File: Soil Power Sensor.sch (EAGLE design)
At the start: 95 parts, among them J1 12401832E402A, U10 TPS7A20330PDBVR, U11 TPS60403DBVR, U12 REF1933AIDDCR, U13 TLV1117LV33DCYR, U14 FSA2466UMX, U2 FT234XD-R, U3 MAX9944ATA+T, U4 ESP32-C3-MINI-1-N4, U5 LTC6362CDDPBF, U6 LTC6362CDDPBF, U7 INA296A5, U8 MAX11201AEUB+, U9 MAX11201AEUB+, X1 SMA-142-0701-801/806

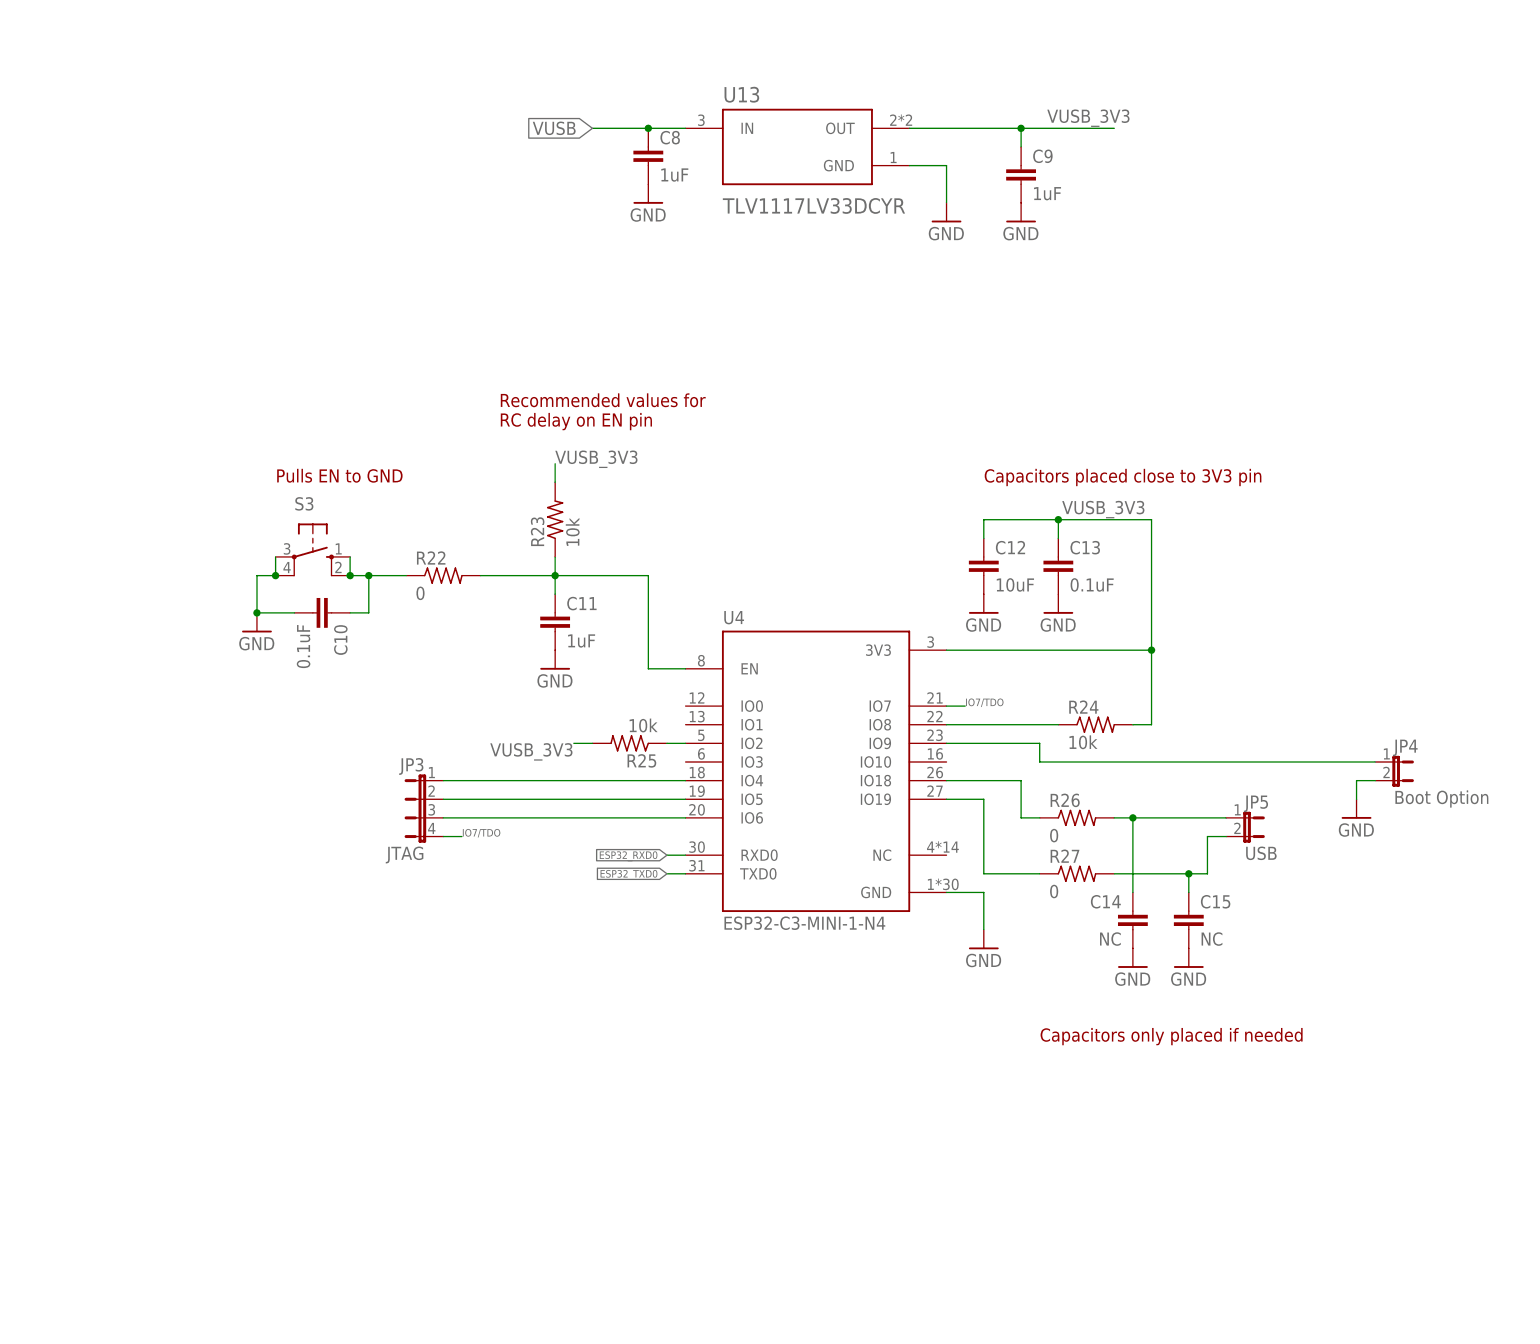
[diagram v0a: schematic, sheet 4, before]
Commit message: Updated JTAG connector for ESP32
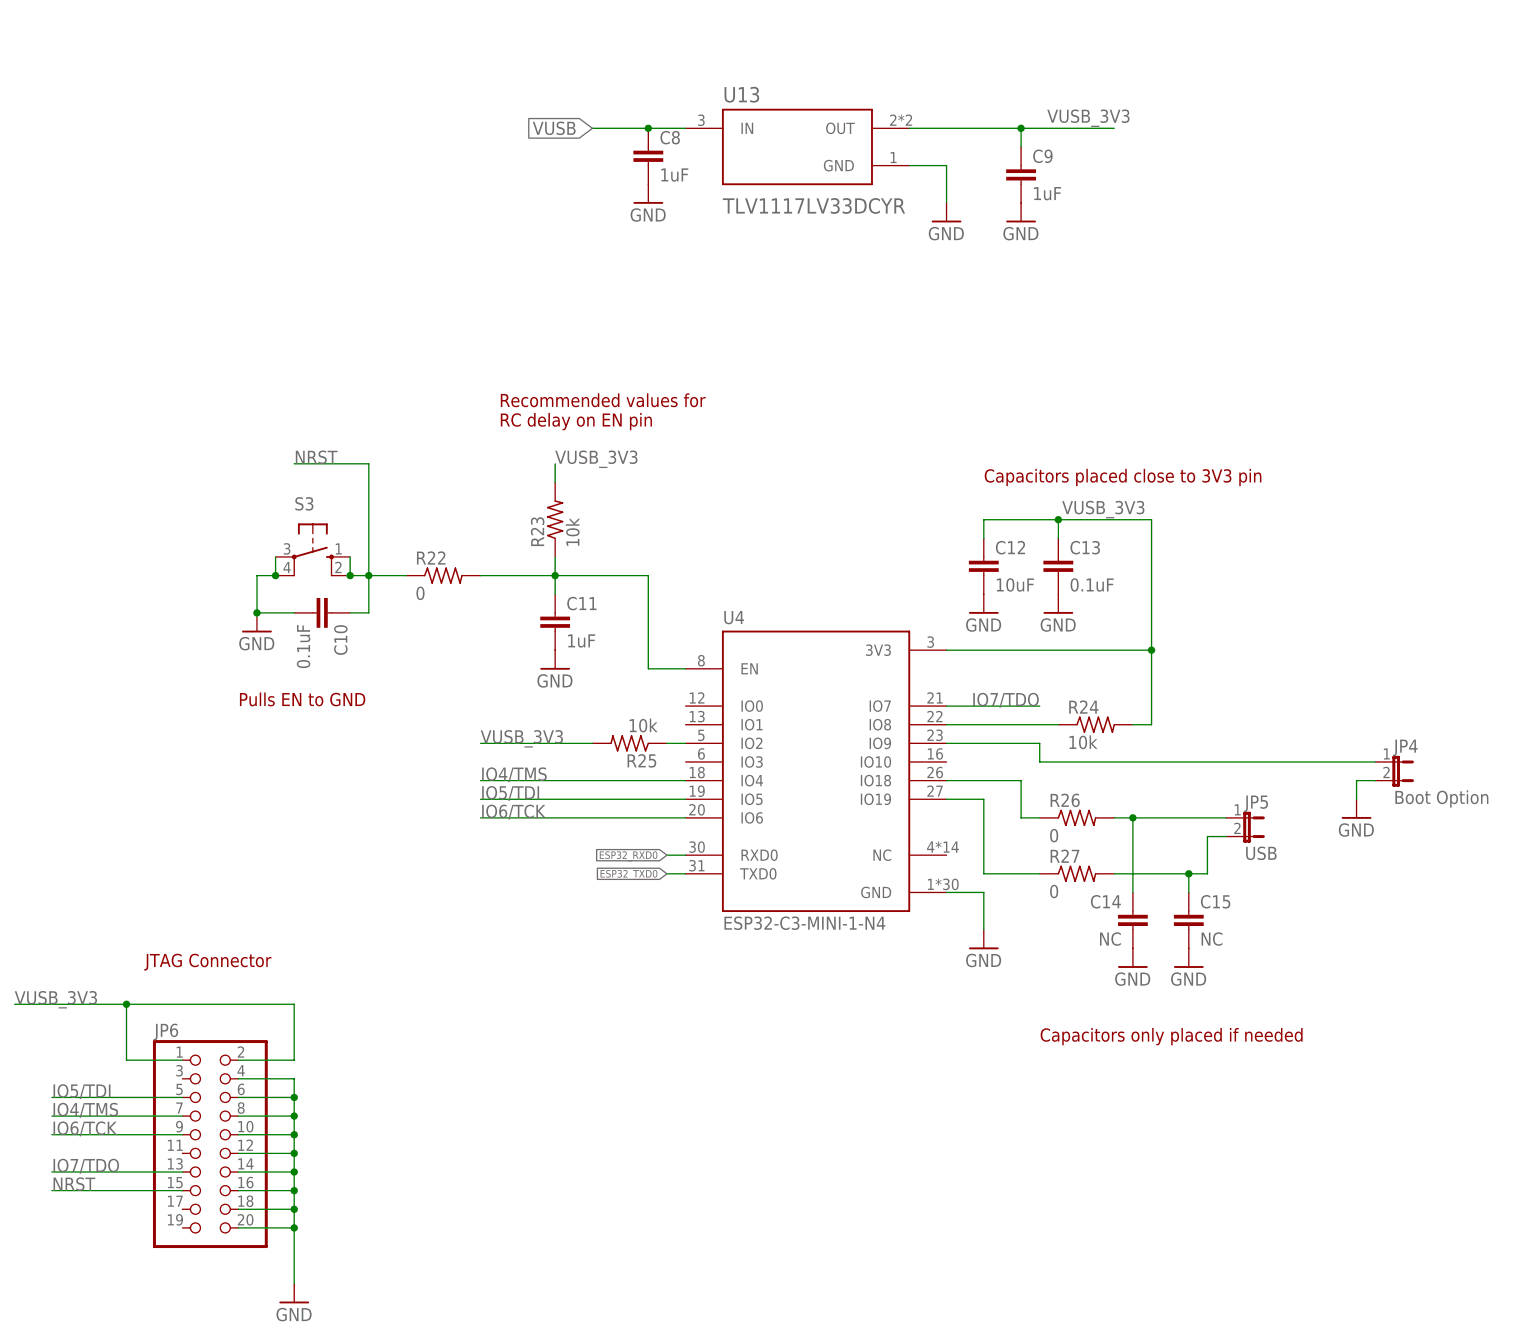
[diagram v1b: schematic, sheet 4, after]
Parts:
- removed JP3: JTAG, jumper:JP4E
- added JP6: (no value), pinhead:PINHD-2X10
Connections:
- removed net N$22: C10.1, R22.1, S3.S, S3.S1
- net GND: now also JP6.10, JP6.12, JP6.14, JP6.16, JP6.18, JP6.20, JP6.4, JP6.6, JP6.8
- net IO4/TMS: now also JP6.7; no longer JP3.1
- net IO5/TDI: now also JP6.5; no longer JP3.2
- net IO6/TCK: now also JP6.9; no longer JP3.3
- net IO7/TDO: now also JP6.13; no longer JP3.4
- net NRST: now also C10.1, JP6.15, R22.1, S3.S, S3.S1
- net VUSB_3V3: now also JP6.1, JP6.2
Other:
- note added: "JTAG Connector"

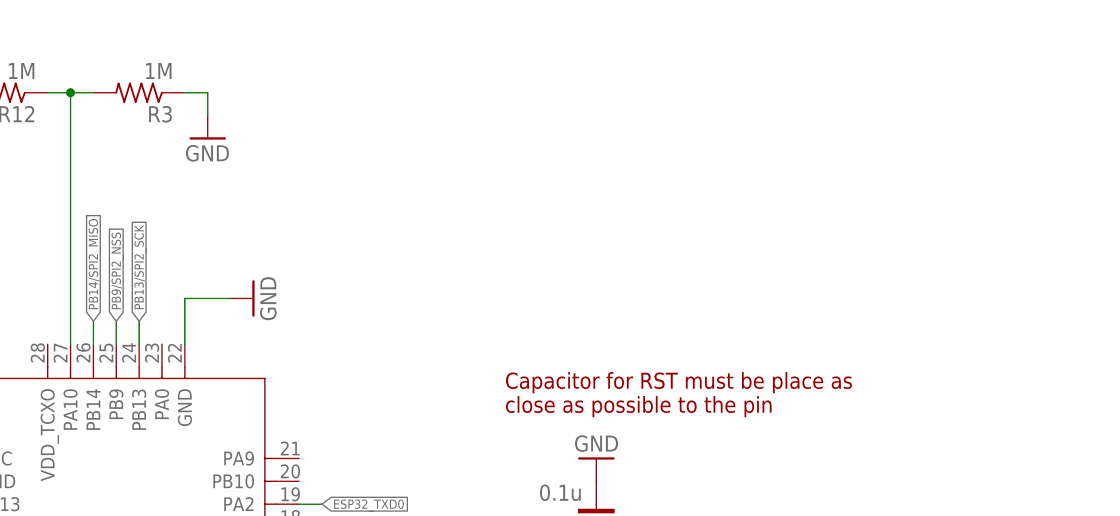
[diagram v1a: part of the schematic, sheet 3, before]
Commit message: Added connection for TEROS-12
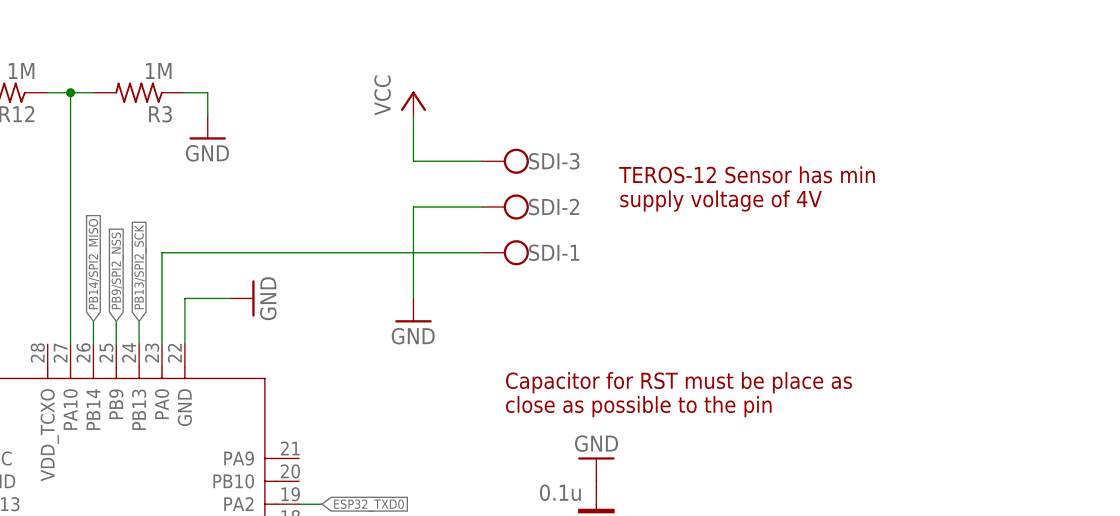
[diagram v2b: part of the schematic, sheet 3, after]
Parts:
- added SDI: (no value), con-wago-500:W237-103
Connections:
- new net N$22: SDI-1.KL, U1.PA0
- net GND: now also SDI-2.KL
- net VCC: now also SDI-3.KL
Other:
- note added: "TEROS-12 Sensor has min supply voltage of 4V"
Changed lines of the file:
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@@
 <part name="JP6" library="pinhead" library_urn="urn:adsk.eagle:library:325" deviceset="PINHD-2X10" device="" package3d_urn="urn:adsk.eagle:package:22405/2"/>
 <part name="GND40" library="supply1" library_urn="urn:adsk.eagle:library:371" deviceset="GND" device=""/>
+<part name="GND41" library="supply1" library_urn="urn:adsk.eagle:library:371" deviceset="GND" device=""/>
+<part name="P+6" library="supply1" library_urn="urn:adsk.eagle:library:371" deviceset="VCC" device=""/>
+<part name="SDI" library="con-wago-500" library_urn="urn:adsk.eagle:library:195" deviceset="W237-103" device="" package3d_urn="urn:adsk.eagle:package:10691/1"/>
 </parts>
 <sheets>
@@
 <text x="193.04" y="162.56" size="1.778" layer="94">Resistor in case NRST does
 not work as expected</text>
+<text x="124.46" y="187.96" size="1.778" layer="94">TEROS-12 Sensor has min
+supply voltage of 4V</text>
 </plain>
 <instances>
@@
 <attribute name="NAME" x="191.77" y="174.2186" size="1.778" layer="95"/>
 <attribute name="VALUE" x="191.77" y="169.418" size="1.778" layer="96"/>
+</instance>
+<instance part="GND41" gate="1" x="101.6" y="175.26" smashed="yes">
+<attribute name="VALUE" x="99.06" y="172.72" size="1.778" layer="96"/>
+</instance>
+<instance part="P+6" gate="VCC" x="101.6" y="200.66" smashed="yes">
+<attribute name="VALUE" x="99.06" y="198.12" size="1.778" layer="96" rot="R90"/>
+</instance>
+<instance part="SDI" gate="-1" x="114.3" y="182.88" smashed="yes" rot="R180">
+<attribute name="NAME" x="114.3" y="181.991" size="1.778" layer="95"/>
+</instance>
+<instance part="SDI" gate="-2" x="114.3" y="187.96" smashed="yes" rot="R180">
+<attribute name="NAME" x="114.3" y="187.071" size="1.778" layer="95"/>
+</instance>
+<instance part="SDI" gate="-3" x="114.3" y="193.04" smashed="yes" rot="R180">
+<attribute name="VALUE" x="116.84" y="196.723" size="1.778" layer="96" rot="R180"/>
+<attribute name="NAME" x="114.3" y="192.151" size="1.778" layer="95"/>
 </instance>
 </instances>
@@
 <junction x="246.38" y="185.42"/>
 </segment>
+<segment>
+<pinref part="GND41" gate="1" pin="GND"/>
+<wire x1="101.6" y1="187.96" x2="101.6" y2="177.8" width="0.1524" layer="91"/>
+<pinref part="SDI" gate="-2" pin="KL"/>
+<wire x1="109.22" y1="187.96" x2="101.6" y2="187.96" width="0.1524" layer="91"/>
+</segment>
 </net>
 <net name="N$2" class="0">
@@
 <junction x="223.52" y="198.12"/>
 </segment>
+<segment>
+<pinref part="P+6" gate="VCC" pin="VCC"/>
+<wire x1="101.6" y1="193.04" x2="101.6" y2="198.12" width="0.1524" layer="91"/>
+<pinref part="SDI" gate="-3" pin="KL"/>
+<wire x1="109.22" y1="193.04" x2="101.6" y2="193.04" width="0.1524" layer="91"/>
+</segment>
 </net>
 <net name="PB4/CTS/JNTRST" class="0">
@@
 </segment>
 </net>
+<net name="N$22" class="0">
+<segment>
+<pinref part="U1" gate="G$1" pin="PA0"/>
+<wire x1="109.22" y1="182.88" x2="73.66" y2="182.88" width="0.1524" layer="91"/>
+<wire x1="73.66" y1="182.88" x2="73.66" y2="172.72" width="0.1524" layer="91"/>
+<pinref part="SDI" gate="-1" pin="KL"/>
+</segment>
+</net>

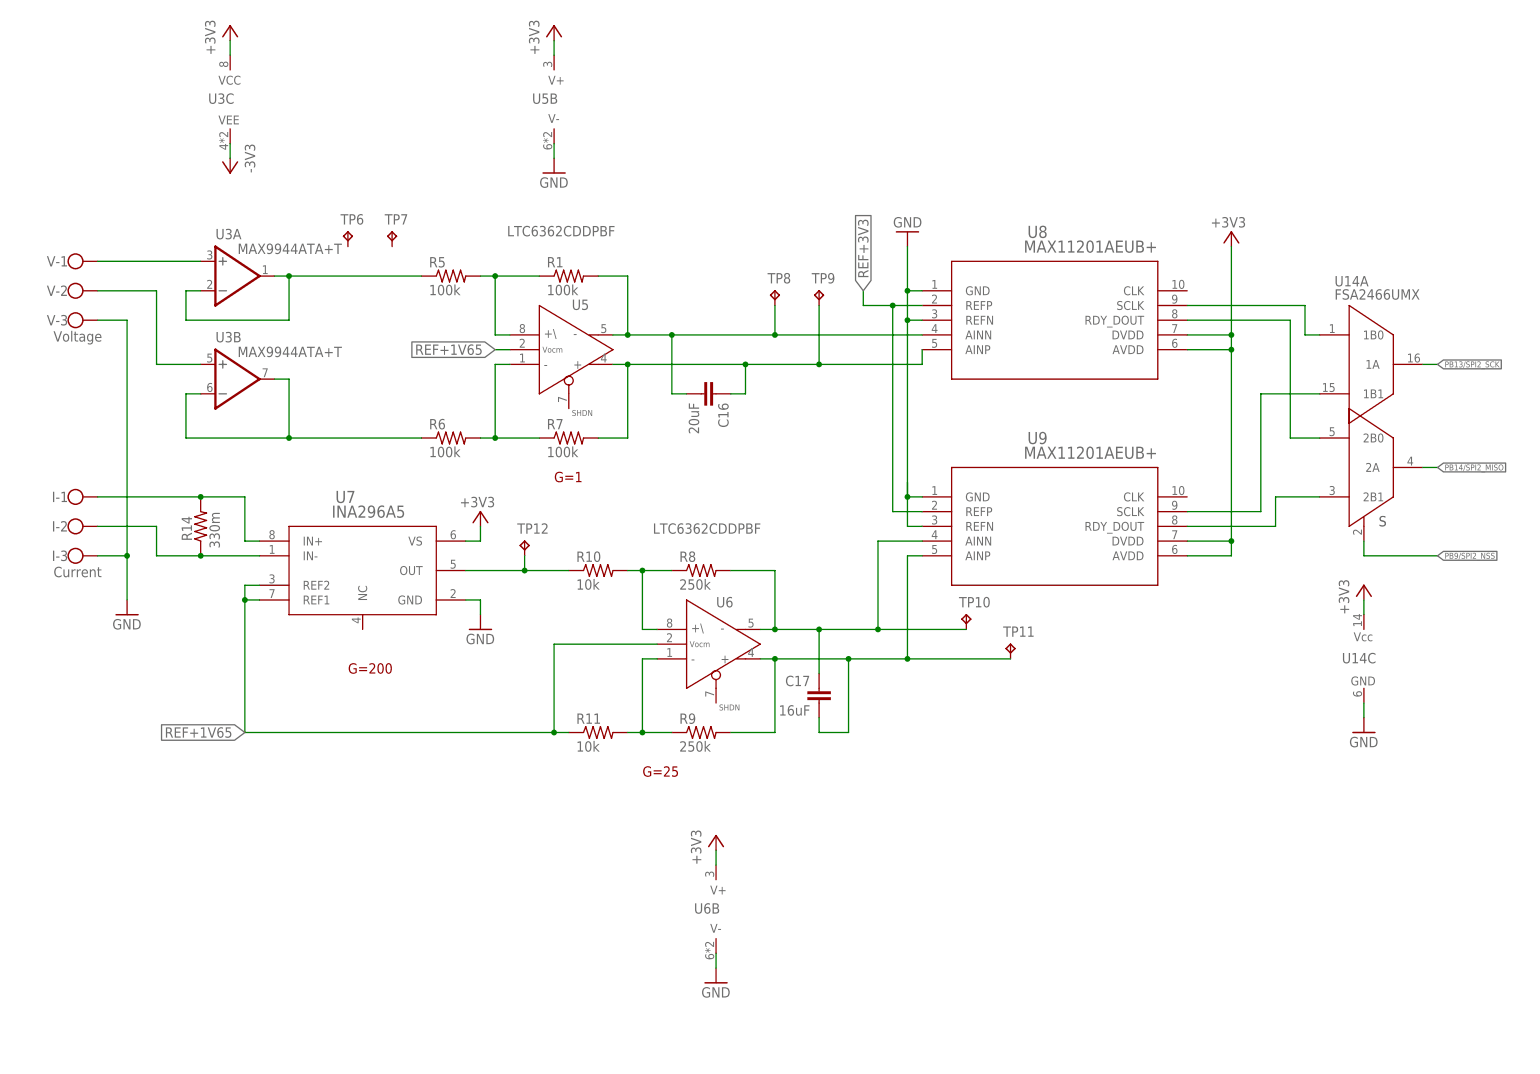
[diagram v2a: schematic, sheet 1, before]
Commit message: Added in-situ Rload
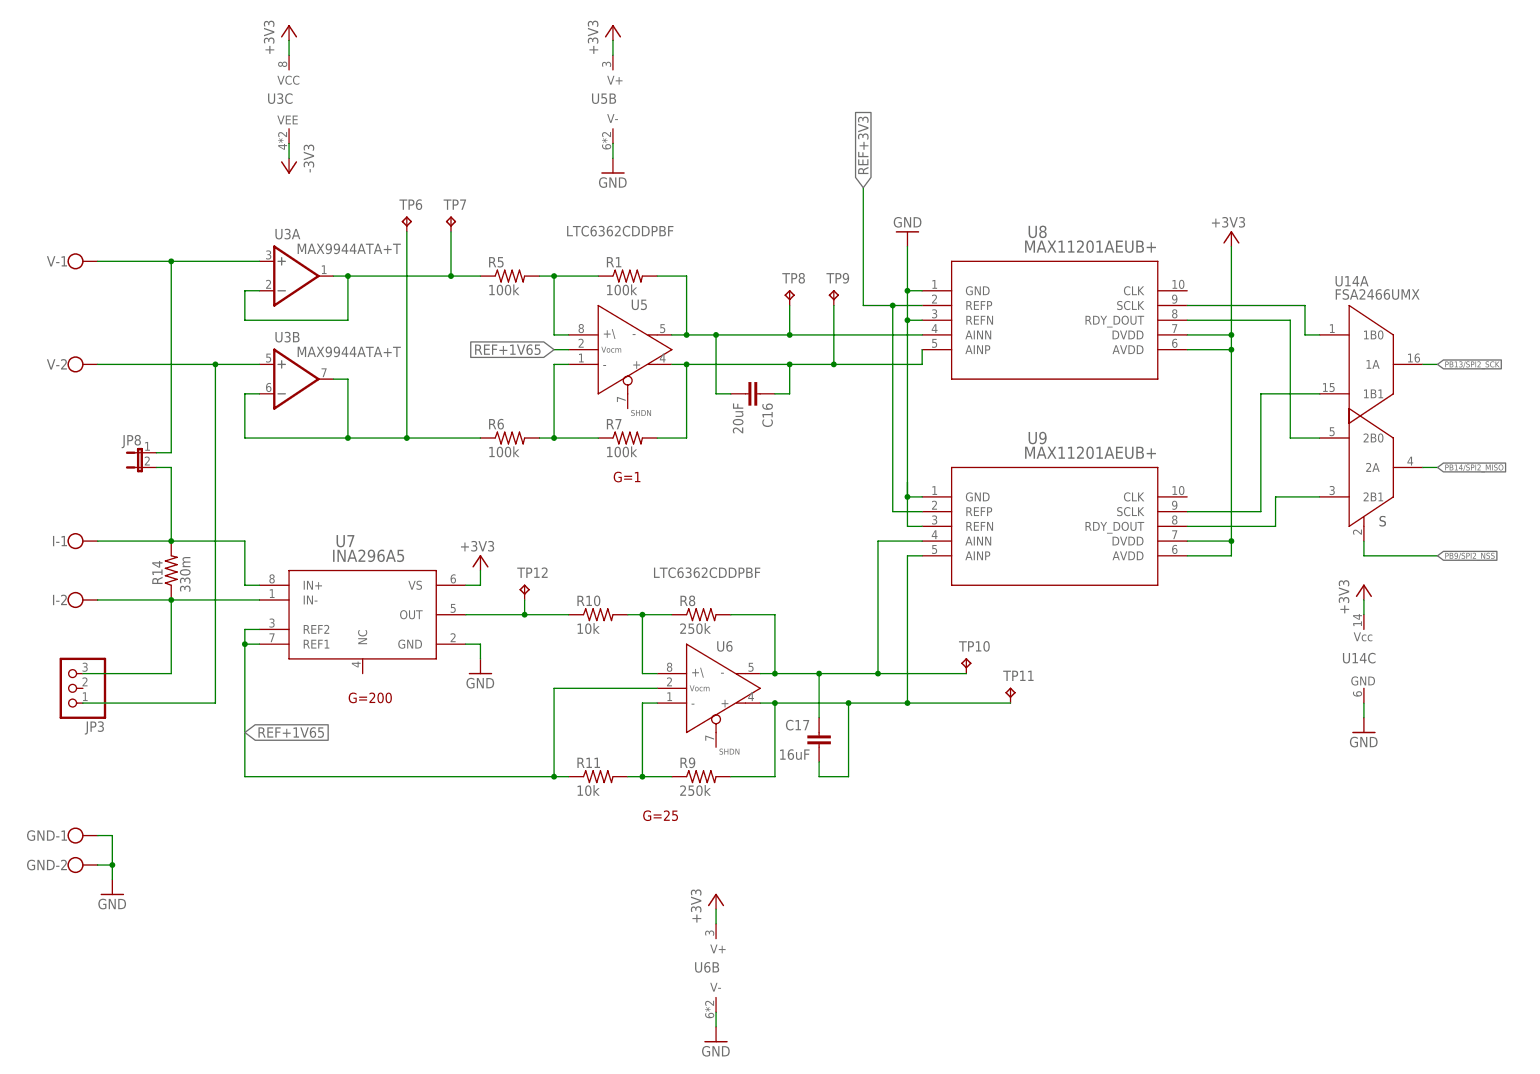
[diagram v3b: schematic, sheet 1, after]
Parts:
- added GND: (no value), con-wago-500:W237-102
- added JP3: (no value), pinhead:PINHD-1X3
- added JP8: (no value), jumper:JP1E
- I: value Current -> (none); device con-wago-500:W237-103 -> con-wago-500:W237-102
- V: value Voltage -> (none); device con-wago-500:W237-103 -> con-wago-500:W237-102
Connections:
- removed net N$5: U3B.+IN, V-2.KL
- new net N$46: JP3.1, U3B.+IN, V-2.KL
- net GND: now also GND-1.KL, GND-2.KL; no longer I-3.KL, V-3.KL
- net N$1: now also JP8.1
- net N$20: now also TP6.TP
- net N$38: now also JP3.3
- net N$4: now also TP7.TP
- net N$45: now also JP8.2
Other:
- note added: "Strong LDO to power ESP32 (max 500mA) LDO can supply max 1A"
- moved on the sheet: C16, C17, I-1, I-2, R1, R10, R11, R14, R5, R6, R7, R8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
